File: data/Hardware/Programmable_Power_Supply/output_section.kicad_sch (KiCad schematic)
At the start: 17 parts, among them Q3 BSC050N03LS_G, Q4 BSC050N03LS_G, Q5 2N7002, U4 LM5145

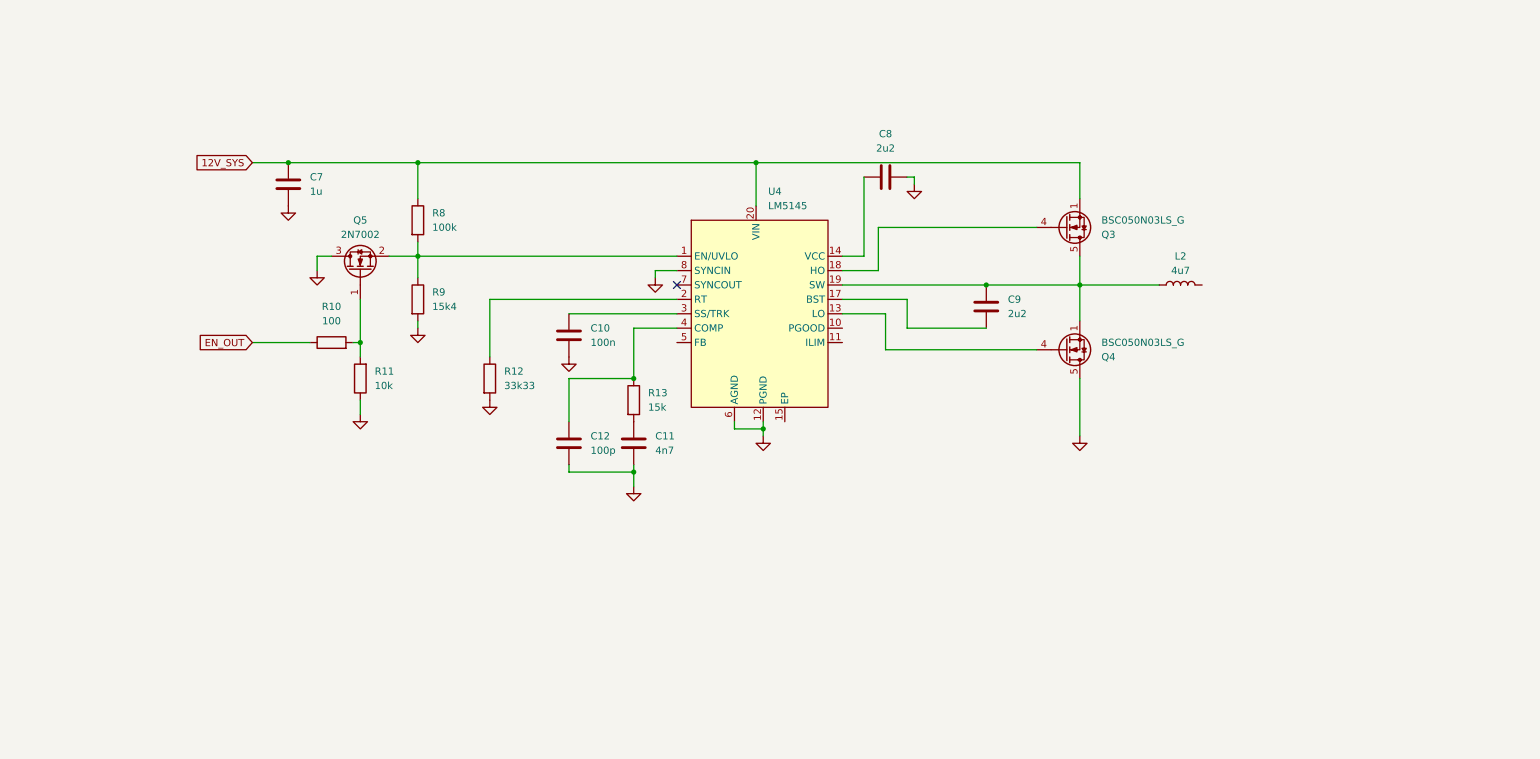
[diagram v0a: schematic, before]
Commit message: feat: First draw of full schematic with all footprints and symbols.
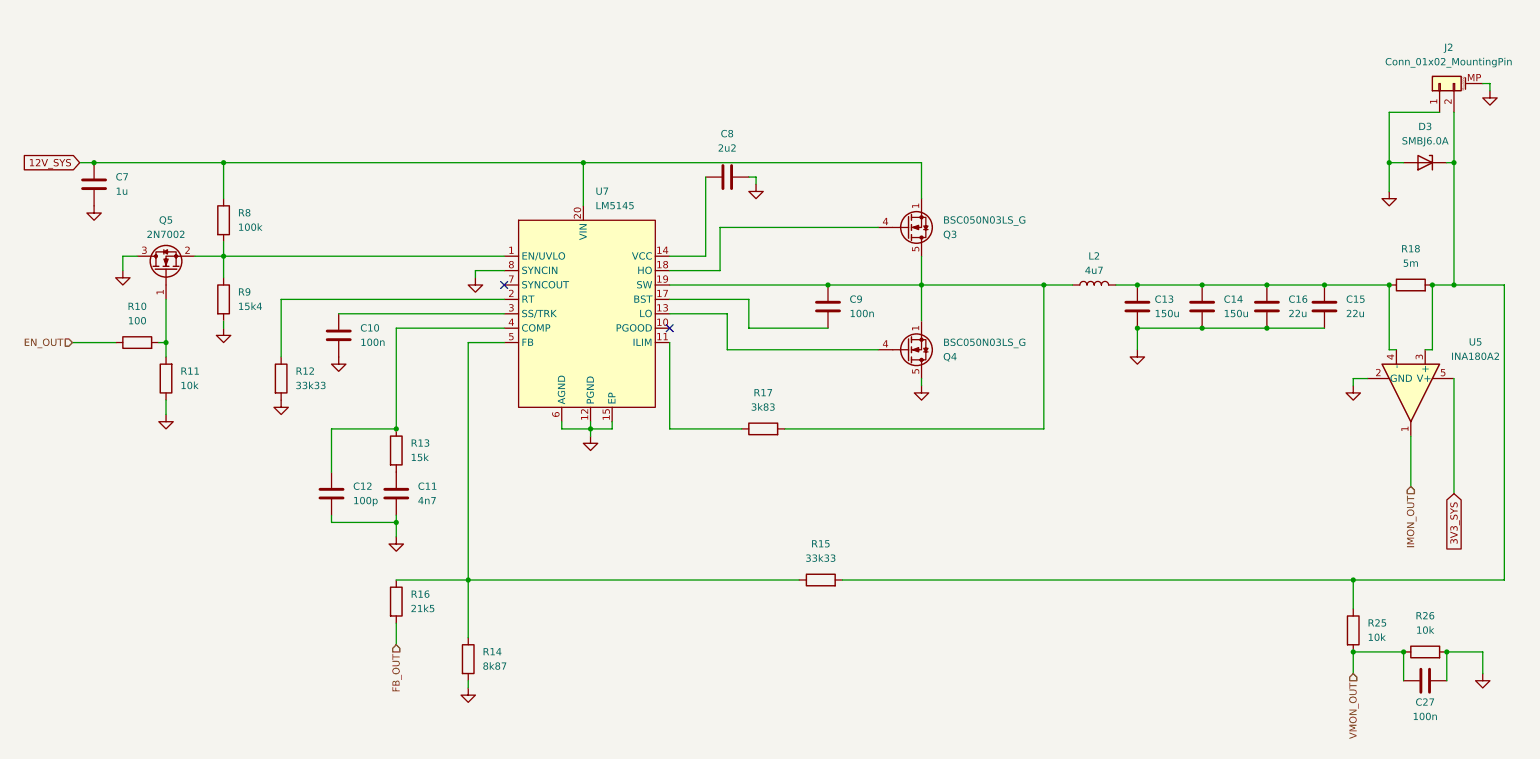
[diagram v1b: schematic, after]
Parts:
- removed U4: LM5145, Szymon_Piorun_Library:RGY0020B, symbol Szymon_Piorun_library:U
- added C13, C14: 150u, Capacitor_Tantalum_SMD:CP_EIA-7343-31_Kemet-D_HandSolder, symbol Device:C
- added C15, C16: 22u, Capacitor_SMD:C_1206_3216Metric_Pad1.33x1.80mm_HandSolder, symbol Device:C
- added C27: 100n, Capacitor_SMD:C_0805_2012Metric_Pad1.18x1.45mm_HandSolder, symbol Device:C
- added D3: SMBJ6.0A, Diode_SMD:D_SMB_Handsoldering, symbol Szymon_Piorun_library:SMBJ6.0A
- added J2: Conn_01x02_MountingPin, Connector_AMASS:AMASS_XT30PW-F_1x02_P2.50mm_Horizontal, symbol Connector_Generic_MountingPin:Conn_01x02_MountingPin
- added R14: 8k87, Resistor_SMD:R_0603_1608Metric_Pad0.98x0.95mm_HandSolder, symbol Device:R
- added R15: 33k33, Resistor_SMD:R_0603_1608Metric_Pad0.98x0.95mm_HandSolder, symbol Device:R
- added R16: 21k5, Resistor_SMD:R_0603_1608Metric_Pad0.98x0.95mm_HandSolder, symbol Device:R
- added R17: 3k83, Resistor_SMD:R_0603_1608Metric_Pad0.98x0.95mm_HandSolder, symbol Device:R
- added R18: 5m, Resistor_SMD:R_2512_6332Metric_Pad1.40x3.35mm_HandSolder, symbol Device:R
- added R25, R26: 10k, Resistor_SMD:R_0603_1608Metric_Pad0.98x0.95mm_HandSolder, symbol Device:R
- added U5: INA180A2, Package_TO_SOT_SMD:SOT-23-5, symbol Amplifier_Current:INA180A2
- added U7: LM5145, Szymon_Piorun_Library:RGY0020B, symbol Szymon_Piorun_library:LM5145
- C10, C11, C12, C7: footprint (none) -> Capacitor_SMD:C_0805_2012Metric_Pad1.18x1.45mm_HandSolder
- C8: footprint (none) -> Capacitor_SMD:C_1206_3216Metric_Pad1.33x1.80mm_HandSolder
- C9: value 2u2 -> 100n; footprint (none) -> Capacitor_SMD:C_0805_2012Metric_Pad1.18x1.45mm_HandSolder
- L2: footprint (none) -> Inductor_SMD:L_TaiTech_TMPC1265_13.5x12.5mm
- R10, R11, R12, R13, R8, R9: footprint (none) -> Resistor_SMD:R_0603_1608Metric_Pad0.98x0.95mm_HandSolder
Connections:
- net 12V_SYS: now also U7.20 (VIN)
- net GND: now also C13.1, C14.1, C15.1, C16.1, C27.1, D3.2 (A), J2.1 (Pin_1), J2.MP (MountPin), R14.2, R26.2, U5.2 (GND), U7.12 (PGND), U7.15 (EP), U7.6 (AGND), U7.8 (SYNCIN)
- net at C12.1, R13.1: now also U7.4 (COMP)
- net at C9.1: now also U7.17 (BST)
- net at C9.2, L2.1, Q3.5 (D)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: now also R17.2, U7.19 (SW)
- net at L2.2: now also C13.2, C14.2, C15.2, C16.2, R18.1, U5.4 (-)
- net at Q3.4 (G): now also U7.18 (HO)
- net at Q5.2 (S), R8.2, R9.1: now also U7.1 (EN/UVLO)
- net at C10.1: now also U7.3 (SS/TRK)
- net at C8.1: now also U7.14 (VCC)
- net at R12.1: now also U7.2 (RT)
- net at Q4.4 (G): now also U7.13 (LO)
- new net: D3.1 (K), J2.2 (Pin_2), R15.2, R18.2, R25.1, U5.3 (+)
- new net: R17.1, U7.11 (ILIM)
- new net: R14.1, R15.1, R16.1, U7.5 (FB)
- new net 3V3_SYS: U5.5 (V+)
- new net FB_OUT: R16.2
- new net IMON_OUT: U5.1
- new net VMON_OUT: C27.2, R25.2, R26.1
- no-connect marks 1 -> 2
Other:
- moved on the sheet: C10, C11, C12, C7, C8, C9, L2, Q3, Q4, Q5, R10, R11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

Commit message: feat: Final version of revision A of the schematic with mouser product numbers attached.
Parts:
- removed C12: 100p, Capacitor_SMD:C_0805_2012Metric_Pad1.18x1.45mm_HandSolder, symbol Device:C
- removed C13, C14: 150u, Capacitor_Tantalum_SMD:CP_EIA-7343-31_Kemet-D_HandSolder, symbol Device:C
- removed J2: Conn_01x02_MountingPin, Connector_AMASS:AMASS_XT30PW-F_1x02_P2.50mm_Horizontal, symbol Connector_Generic_MountingPin:Conn_01x02_MountingPin
- added C13, C14: 150u, Szymon_Piorun_Library:CAPPM7343X310N, symbol Device:C_Polarized
- added J2: Phoenix Contact 1891519, Szymon_Piorun_Library:2 pin power connector, symbol Connector:Conn_01x04_Socket
- C10, C27, C9: footprint Capacitor_SMD:C_0805_2012Metric_Pad1.18x1.45mm_HandSolder -> Capacitor_SMD:C_0201_0603Metric_Pad0.64x0.40mm_HandSolder; Mouser (none) -> MLASG063SB5104KFNA01
- C11: Mouser (none) -> KAM21BR72A472KT
- C15, C16: Mouser (none) -> GRM31CC71C226ME11K
- C7: value 1u -> 2u2; footprint Capacitor_SMD:C_0805_2012Metric_Pad1.18x1.45mm_HandSolder -> Capacitor_SMD:C_1206_3216Metric_Pad1.33x1.80mm_HandSolder; Mouser (none) -> 885382208016
- C8: Mouser (none) -> 885382208016
- D3: Mouser (none) -> SMBJ6.0A
- L2: footprint Inductor_SMD:L_TaiTech_TMPC1265_13.5x12.5mm -> Inductor_SMD:L_Wuerth_WE-GF-1210; Mouser (none) -> 7443320470
- Q3, Q4: footprint Package_SON:Infineon_PG-TDSON-8_6.15x5.15mm -> Szymon_Piorun_Library:Infineon_PG-TDSON-8_6.15x5.15mm; Mouser (none) -> BSC030N03LS G
- Q5: Mouser (none) -> 2N7002
- R10: Mouser (none) -> RT0603BRB07100RL
- R11, R25, R26: Mouser (none) -> RCA060310K0FKEC
- R12, R15: value 33k33 -> 33k; Mouser (none) -> RCA060333K0FKEA
- R13: Mouser (none) -> MCT06030C1502FPW00
- R14: Mouser (none) -> 560112116137
- R16: Mouser (none) -> CRT0603-FZ-2152ELF
- R17: value 3k83 -> 3k8; Mouser (none) -> RN73R1JTTD3282F100
- R18: Mouser (none) -> WSLP25125L000FEA
- R8: Mouser (none) -> RCA0603100KFKEC
- R9: value 15k4 -> 15k; Mouser (none) -> MCT06030C1502FPW00
- U5: Mouser (none) -> INA180A2IDBVR
- U7: Mouser (none) -> LM5145RGYR
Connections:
- net 12V_SYS: now also C7.2; no longer C7.1
- net EN_OUT: now also R10.2; no longer R10.1
- net GND: now also C15.2, C16.2, C27.2, C7.1, C13.2, C14.2, J2.1 (Pin_1), J2.2 (Pin_2); no longer C15.1, C16.1, C27.1, C7.2
- net VMON_OUT: now also C27.1; no longer C27.2
- net at D3.1 (K), R15.2, R18.2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: now also J2.3 (Pin_3), J2.4 (Pin_4)
- net at L2.2, R18.1, U5.4 (-): now also C15.1, C16.1, C13.1, C14.1; no longer C15.2, C16.2
- net at L2.1, Q3.5 (D), Q3.6 (D)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: now also C9.1; no longer C9.2
- net at Q5.1 (G), R11.2: now also R10.1; no longer R10.2
- net at U7.17 (BST): now also C9.2; no longer C9.1

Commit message: feat: First full layout of the PCB
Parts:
- added C26: 2u2, Capacitor_SMD:C_1206_3216Metric_Pad1.33x1.80mm_HandSolder, symbol Device:C
- L2: footprint Inductor_SMD:L_Wuerth_WE-GF-1210 -> Inductor_SMD:L_Wuerth_HCI-1365; Mouser 7443320470 -> 7443551470
- Q3, Q4: Mouser BSC030N03LS G -> (none)
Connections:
- net 12V_SYS: now also Q3.5 (D), C26.2; no longer Q3.1 (S), Q3.2 (S), Q3.3 (S)
- net GND: now also Q4.1 (S), Q4.2 (S), Q4.3 (S), Q5.2 (S), C26.1; no longer Q4.5 (D), Q4.6 (D), Q4.7 (D), Q4.8 (D), Q5.3 (D)
- net V_OUT: now reaches D3.1 (K), J2.3 (Pin_3), J2.4 (Pin_4), R15.2, R18.2, R25.1, U5.3 (+)
- net V_OUT_PMON: now reaches C13.1, C14.1, C15.1, C16.1, L2.2, R18.1, U5.4 (-)
- net LM_COMP: now reaches R13.1, U7.4 (COMP)
- net LM_EN/UVLO: now reaches R8.2, R9.1, U7.1 (EN/UVLO)
- net LM_EN/UVLO: now also Q5.3 (D); no longer Q5.2 (S)
- net LM_LO: now reaches Q4.4 (G), U7.13 (LO)
- net LM_VCC: now reaches C8.1, U7.14 (VCC)
- net LM_FB: now reaches R14.1, R15.1, R16.1, U7.5 (FB)
- net LM_BST: now reaches C9.2, U7.17 (BST)
- net LM_HO: now reaches Q3.4 (G), U7.18 (HO)
- net LM_RT: now reaches R12.1, U7.2 (RT)
- net LM_SS: now reaches C10.1, U7.3 (SS/TRK)
- new net LM_ILIM: C9.1, L2.1, Q3.1 (S), Q3.2 (S), Q3.3 (S), Q4.5 (D), R17.2, U7.19 (SW)
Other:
- moved on the sheet: D3, J2, Q5
